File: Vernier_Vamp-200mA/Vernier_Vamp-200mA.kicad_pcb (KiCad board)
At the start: 4 copper layers, 160 x 99.5 mm, 209 parts, among them J1 Conn_01x02, J2 RJ45, J3 Screw_Terminal_01x04, J4 Conn_02x07_Odd_Even, J5 Channel 3, J6 Channel 2, J7 Channel 1, Q1 Si4447ADY, Q2 IRF8707PbF, SW1 DPDT_Hirose, U1 LM4040DBZ-5, U10 OPA2277, U11 OPA2277, U12 OPA2277, U13 OPA2277, U14 OPA2277, U15 OPA1622, U16 OPA1622, U17 OPA1622, U2 LM4040DBZ-5, U3 LM393, U4 TPS7A470x, U5 TPS7A470x, U6 TPS7A33, U7 LTC6655-2.5, U8 DAC8814, U9 OPA2277

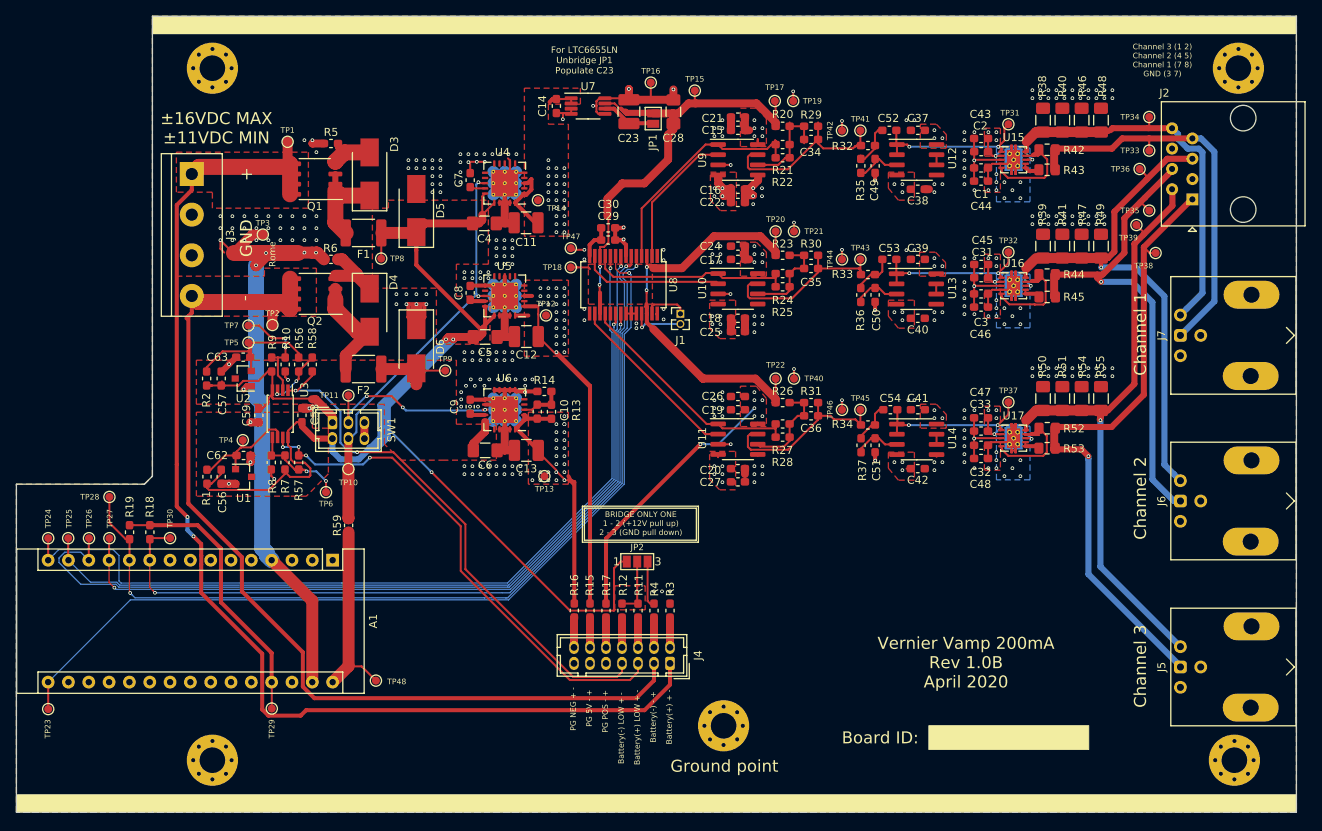
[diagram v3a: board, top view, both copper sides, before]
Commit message: 200mA changes
-Changed OPA1622 footprint to accommodate tented vias
-Rounded edges of the board to reduce mechanical stress
-Refined drawing dimensions
-Added title block to every schematic and layout sheet.
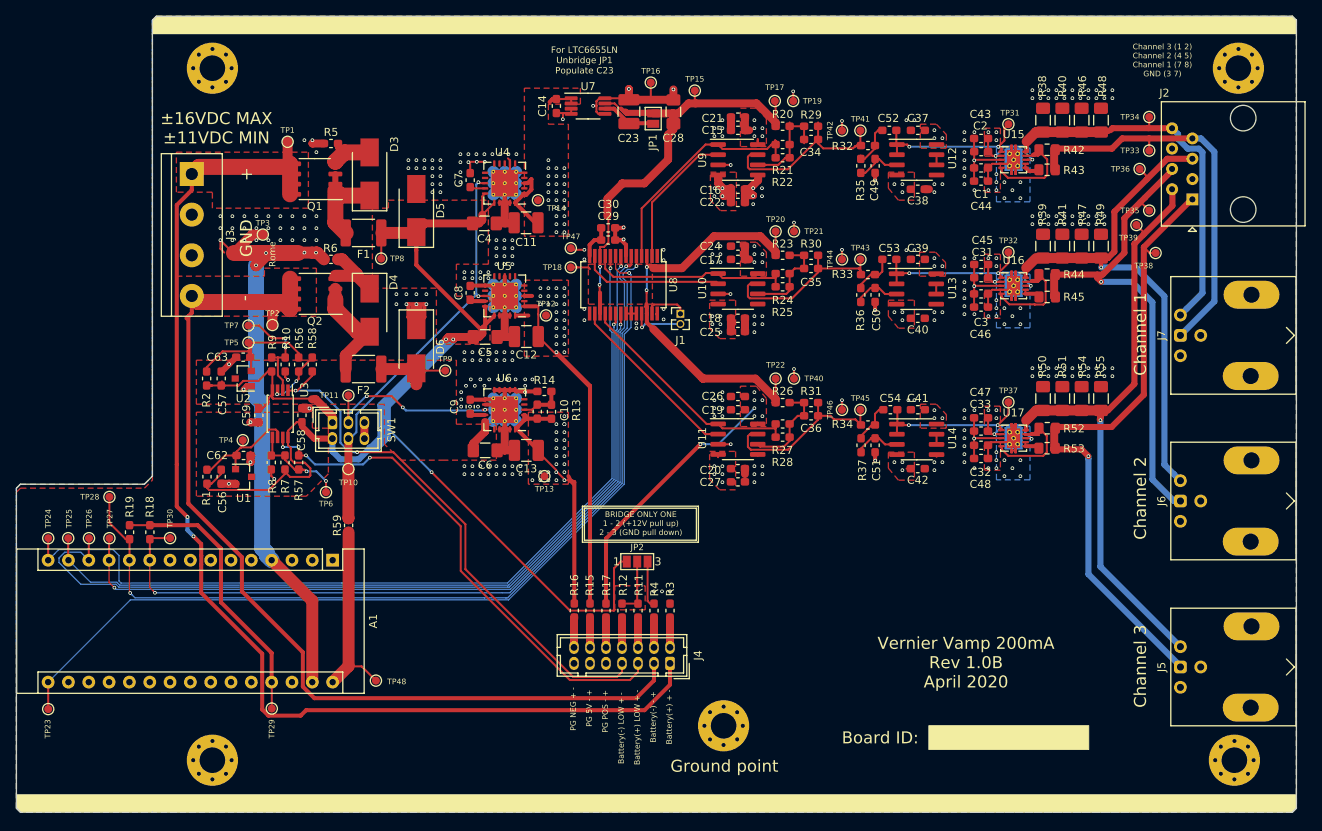
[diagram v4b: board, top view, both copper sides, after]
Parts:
- U15, U16, U17: footprint Package_SON:Texas_S-PVSON-N10_ThermalVias -> PVSON-10_ThermalVias-Tented:Texas_S-PVSON-10_ThermalVias-Tented
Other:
- outline, holes or cut-outs redrawn

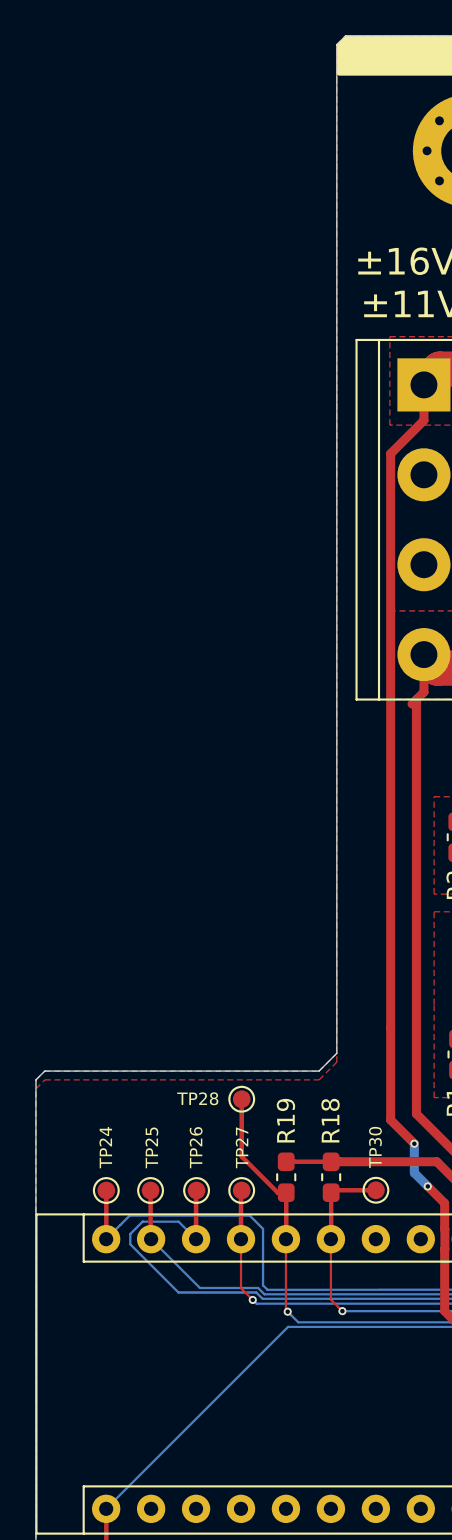
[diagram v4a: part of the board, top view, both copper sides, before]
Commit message: 200mA via fix
-Fixed incorrect assignment of vias
-Re-worked the copper pours
-Updated plotter settings for 200mA and 2mA version
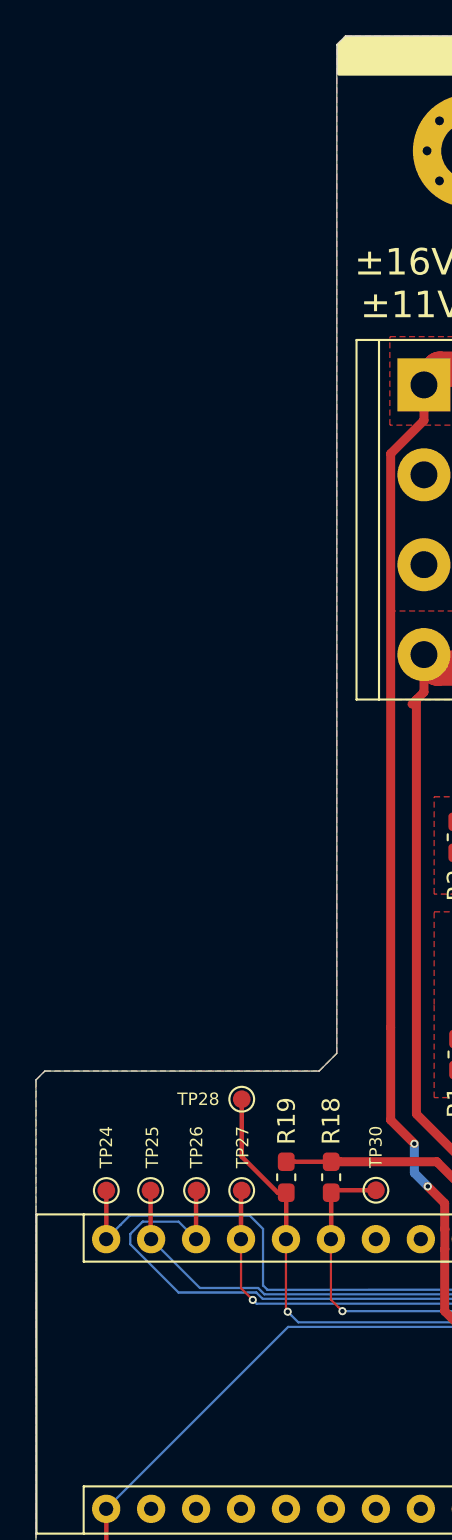
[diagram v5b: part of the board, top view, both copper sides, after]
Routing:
- net GND: vias 321 -> 316
- net +7V5: vias 60 -> 65
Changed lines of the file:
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@@
       (layerselection 0x010fc_ffffffff)
       (usegerberextensions false)
-      (usegerberattributes false)
+      (usegerberattributes true)
       (usegerberadvancedattributes false)
       (creategerberjobfile false)
@@
       (viasonmask false)
       (mode 1)
-      (useauxorigin false)
+      (useauxorigin true)
       (hpglpennumber 1)
       (hpglpenspeed 20)
@@
       (outputformat 1)
       (mirror false)
-      (drillshape 1)
+      (drillshape 0)
       (scaleselection 1)
-      (outputdirectory ""))
+      (outputdirectory "gerber/"))
   )
   (net 0 "")
@@
   (segment (start 87.541 96.94) (end 86.116 98.365) (width 1.5) (layer B.Cu) (net 26))
   (segment (start 87.541 96.94) (end 86.196601 96.94) (width 1.5) (layer B.Cu) (net 26))
-  (via (at 95 68.75) (size 0.4572) (drill 0.254) (layers F.Cu B.Cu) (net 26))
-  (via (at 95 67.75) (size 0.4572) (drill 0.254) (layers F.Cu B.Cu) (net 26))
-  (via (at 95 66.75) (size 0.4572) (drill 0.254) (layers F.Cu B.Cu) (net 26))
-  (via (at 94 66.75) (size 0.4572) (drill 0.254) (layers F.Cu B.Cu) (net 26))
-  (via (at 94 67.75) (size 0.4572) (drill 0.254) (layers F.Cu B.Cu) (net 26))
+  (via (at 95 68.75) (size 0.4572) (drill 0.254) (layers F.Cu B.Cu) (net 96))
+  (via (at 95 67.75) (size 0.4572) (drill 0.254) (layers F.Cu B.Cu) (net 96))
+  (via (at 95 66.75) (size 0.4572) (drill 0.254) (layers F.Cu B.Cu) (net 96))
+  (via (at 94 66.75) (size 0.4572) (drill 0.254) (layers F.Cu B.Cu) (net 96))
+  (via (at 94 67.75) (size 0.4572) (drill 0.254) (layers F.Cu B.Cu) (net 96))
   (segment (start 105.725 121.175) (end 106.2 121.175) (width 0.254) (layer F.Cu) (net 26))
   (segment (start 105.4 120.85) (end 105.725 121.175) (width 0.254) (layer F.Cu) (net 26))
@@
       (pts
         (xy 186.5 48.25) (xy 186.5 146.75) (xy 186 147.25) (xy 146.5 147.25) (xy 106.5 147.25)
-        (xy 27 147.25) (xy 26.5 146.75) (xy 26.5 126.75) (xy 26.5 107.25) (xy 27 106.75)
-        (xy 42.5 106.75) (xy 43.5 105.75) (xy 43.5 48.25) (xy 43.999997 47.75) (xy 115 47.75)
+        (xy 27 147.25) (xy 26.5 146.75) (xy 26.5 126.75) (xy 26.5 106.75) (xy 27 106.25)
+        (xy 42.5 106.25) (xy 43.5 105.25) (xy 43.5 48.25) (xy 43.999997 47.75) (xy 115 47.75)
         (xy 150.75 47.75) (xy 186 47.75)
       )

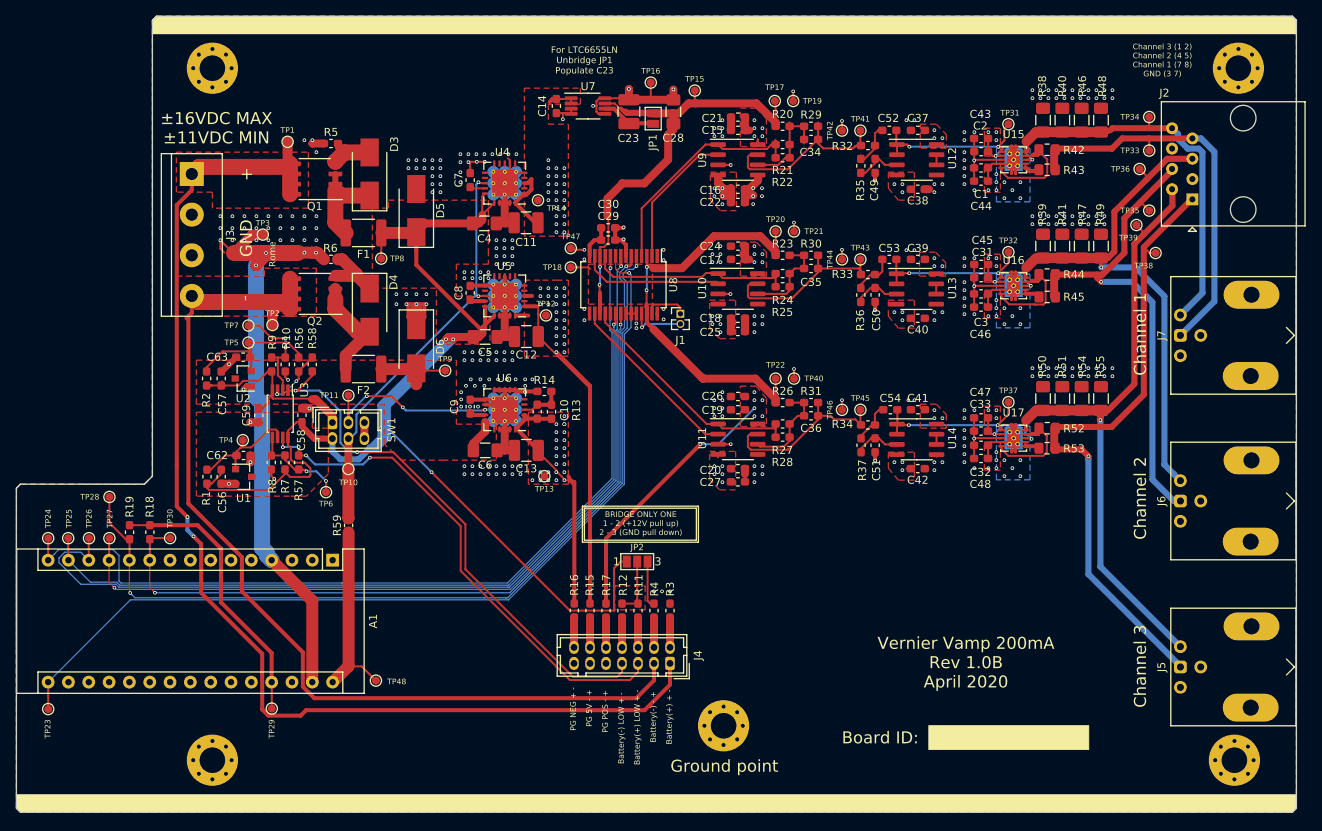
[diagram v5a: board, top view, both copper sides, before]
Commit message: 1.0C Initial commit
-Fixed amplifier output
-Changed connectors to IDC
-Via perimeter added
TODO:
Add shielding over analogue section
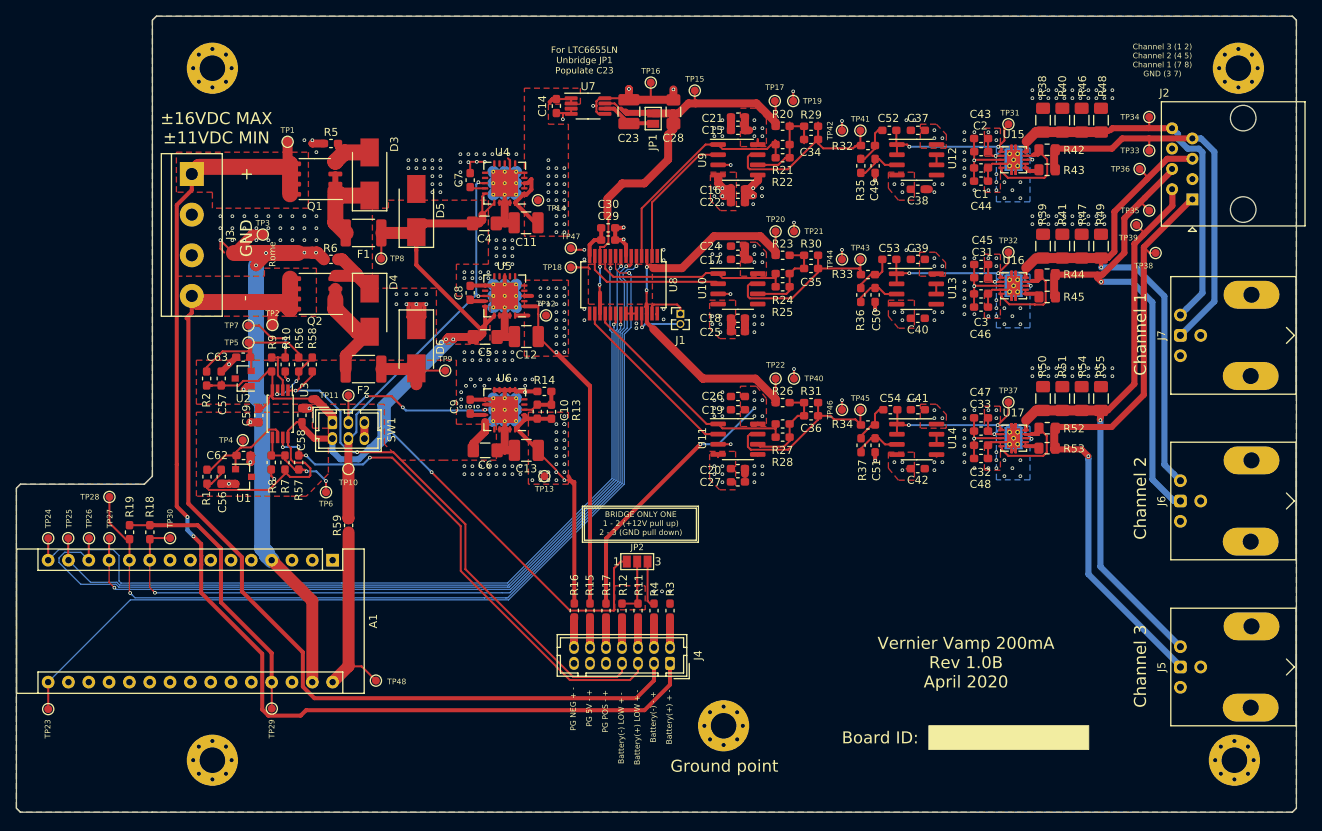
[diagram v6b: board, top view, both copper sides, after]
